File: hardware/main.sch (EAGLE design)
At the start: 69 parts, among them IC1 MPU-6050, IC2 TB6612FNG, Q1 TEFT4300, Q2 TEFT4300, Q3 TEFT4300, Q4 TEFT4300, Q5 TEFT4300, Q6 TEFT4300, Q8 8MHz

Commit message: schematic...
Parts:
- added C8_GRM1, C8_GRM2, C8_GRM3, C8_GRM31: 10u, rcl:C-EUC1206
- added C9_BYPASS, C9_BYPASS1: 100n, rcl:C-EUC0603
- added L1, L2: (no value), rcl:L-EUL5038P
- added Q7: IRLML2244, microbuilder:MOSFET-P
- added R22, R25: (no value), resistor:R-EU_R0805
- added R26, R27, R28, R29: (no value), rcl:R-EU_R0603
- added U$1: PRZELACZNIK_SUWAKOWY, micromouse:PRZELACZNIK_SUWAKOWY
- added U$2, U$3: PINHEAD-1X2, BaseApp:PINHEAD-1X2
- added U$4, U$5: ST1S40, micromouse:ST1S40
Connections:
- new net +7V: R22.2
- new net N$41: U$2.2, U$3.1
- new net N$43: U$1.2, U$1.5, U$3.2
- new net N$46: Q7.S, U$1.3, U$1.6
- new net N$47: L1.1, U$4.SW
- new net N$50: C8_GRM1.1, L1.2, R26.2
- new net N$52: R26.1, R27.2, U$4.FB
- new net N$53: R28.1, R29.2, U$5.FB
- new net N$54: C8_GRM3.1, L2.2, R28.2
- new net N$55: L2.1, U$5.SW
- new net VIN: C8_GRM2.1, C8_GRM31.1, C9_BYPASS.1, C9_BYPASS1.1, Q7.D, U$4.VINA, U$4.VINSW, U$5.VINA, U$5.VINSW
- net ADC_VBAT: now also R22.1, R25.2
- net GND: now also C8_GRM1.2, C8_GRM2.2, C8_GRM3.2, C8_GRM31.2, C9_BYPASS.2, C9_BYPASS1.2, Q7.G, R25.1, R27.1, R29.1, U$2.1, U$4.GND, U$5.GND
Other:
- moved on the sheet: C1, C12, C25, C3, C4, C5, C6, C7, C_VSSA, C_VSSA1, IC1, IC2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

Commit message: cleanup, 3d top mount
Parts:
- R10, R13, R15, R17, R21, R6, R8: value 1R -> 10k
- T1, T2, T3, T4, T5, T6, T8: value (none) -> IRLML0030
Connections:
- net LED5 renamed ENCL_A
- removed net N$1 (its old number): D7.A
- removed net N$11 (its old number): R8.1, T2.G
- removed net N$13 (its old number): D2.A
- removed net N$16: R10.1, T3.G
- removed net N$17: R13.1, T4.G
- removed net N$18: D4.A
- removed net N$21: R15.1, T5.G
- removed net N$22: D5.A
- removed net N$26: R17.1, T6.G
- removed net N$32: R21.1, T8.G
- removed net N$5 (its old number): D3.A
- removed net N$50: C8_GRM1.1, L1.2, R26.2
- removed net N$54: C8_GRM3.1, L2.2, R28.2
- removed net N$6 (its old number): R6.1, T1.G
- removed net N$8 (its old number): D1.A
- removed net VIN: C8_GRM2.1, C8_GRM31.1, C9_BYPASS.1, C9_BYPASS1.1, Q7.D, U$4.VINA, U$4.VINSW, U$5.VINA, U$5.VINSW
- new net ENCLB: U$6.PA1
- new net ENCR_A: U$6.PA15
- new net ENCR_B: U$6.PB3
- new net VCC: C8_GRM3.1, D1.A, D2.A, D3.A, D4.A, D5.A, D7.A, L2.2, R28.2
- net +3V3: now also C8_GRM1.1, L1.2, R26.2
- net +7V: now also C8_GRM2.1, C8_GRM31.1, C9_BYPASS.1, C9_BYPASS1.1, Q7.D, U$4.VINA, U$4.VINSW, U$5.VINA, U$5.VINSW
- net BOOT0: now also U$6.PB8; no longer U$6.PA15
- net BUZZER: now also R21.2, T8.G
- net D_L: now also T1.G; no longer U$6.PA1
- net D_LF: now also R15.2, T5.G; no longer R10.2
- net D_LS: now also R10.2, T3.G; no longer R15.2
- net D_R: now also T2.G
- net D_RF: now also R17.2, T6.G; no longer R13.2
- net D_RS: now also R13.2, T4.G; no longer R17.2, R21.2
- net GND: now also R10.1, R13.1, R15.1, R17.1, R21.1, R6.1, R8.1
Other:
- moved on the sheet: D2, D3, D4, D5, R10, R12, R13, R14, R15, R16, R17, R20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

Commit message: encoder brd
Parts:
- added U$10, U$9: ENCODER_MOUNT, micromouse:ENCODER_MOUNT
- added U$7, U$8: PINHEAD-1X2, BaseApp:PINHEAD-1X2
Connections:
- new net N$14: U$9.CLK
- new net N$15: U$9.MOSI
- new net N$16: U$9.MISO
- new net N$17: U$9.CS
- new net N$18: U$9.A
- new net N$19: U$9.B
- new net N$20: U$9.VCC
- new net N$22: U$10.A
- new net N$24: U$10.B
- new net N$25: U$10.VCC
- new net N$32: U$10.CS
- new net N$42: U$10.MISO
- new net N$44: U$10.MOSI
- new net N$45: U$10.CLK
- net GND: now also U$10.GND, U$9.GND
- net N$37: now also U$8.2
- net N$38: now also U$7.1
- net N$39: now also U$7.2
- net N$40: now also U$8.1
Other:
- moved on the sheet: C12, C5, C6, C7, IC2

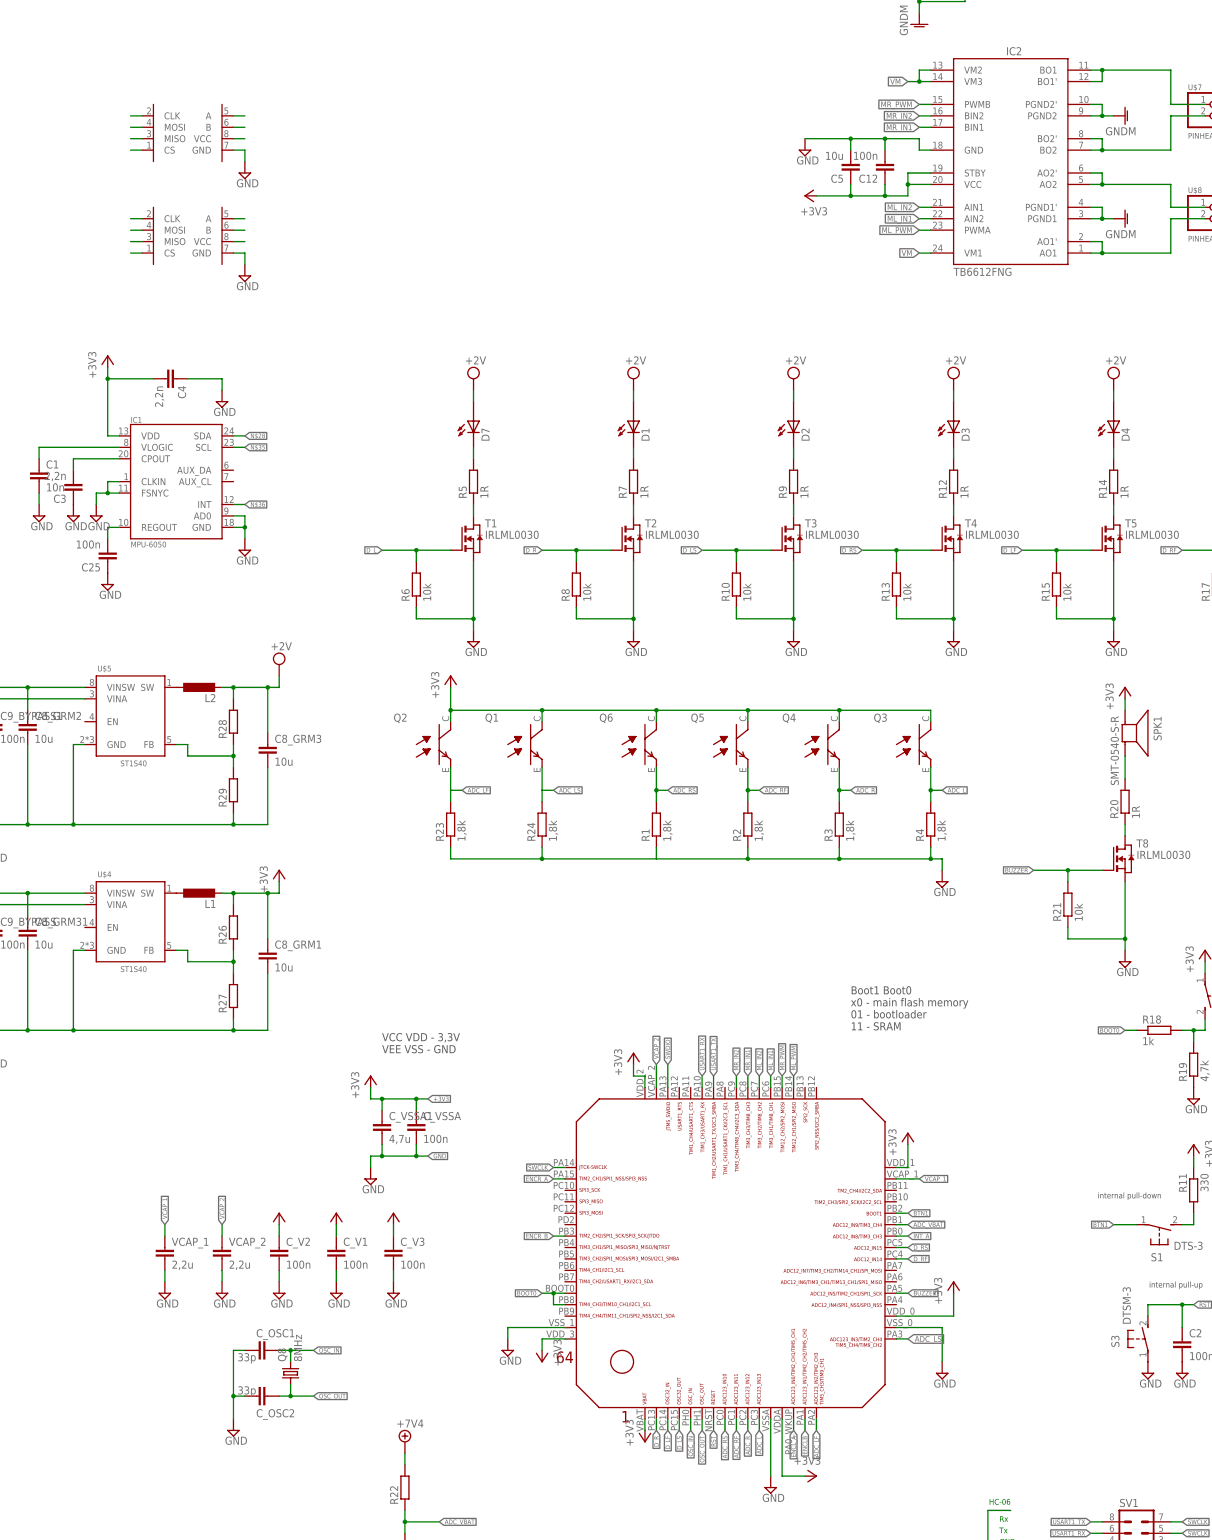
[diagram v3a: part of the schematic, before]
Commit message: fixed 3d model
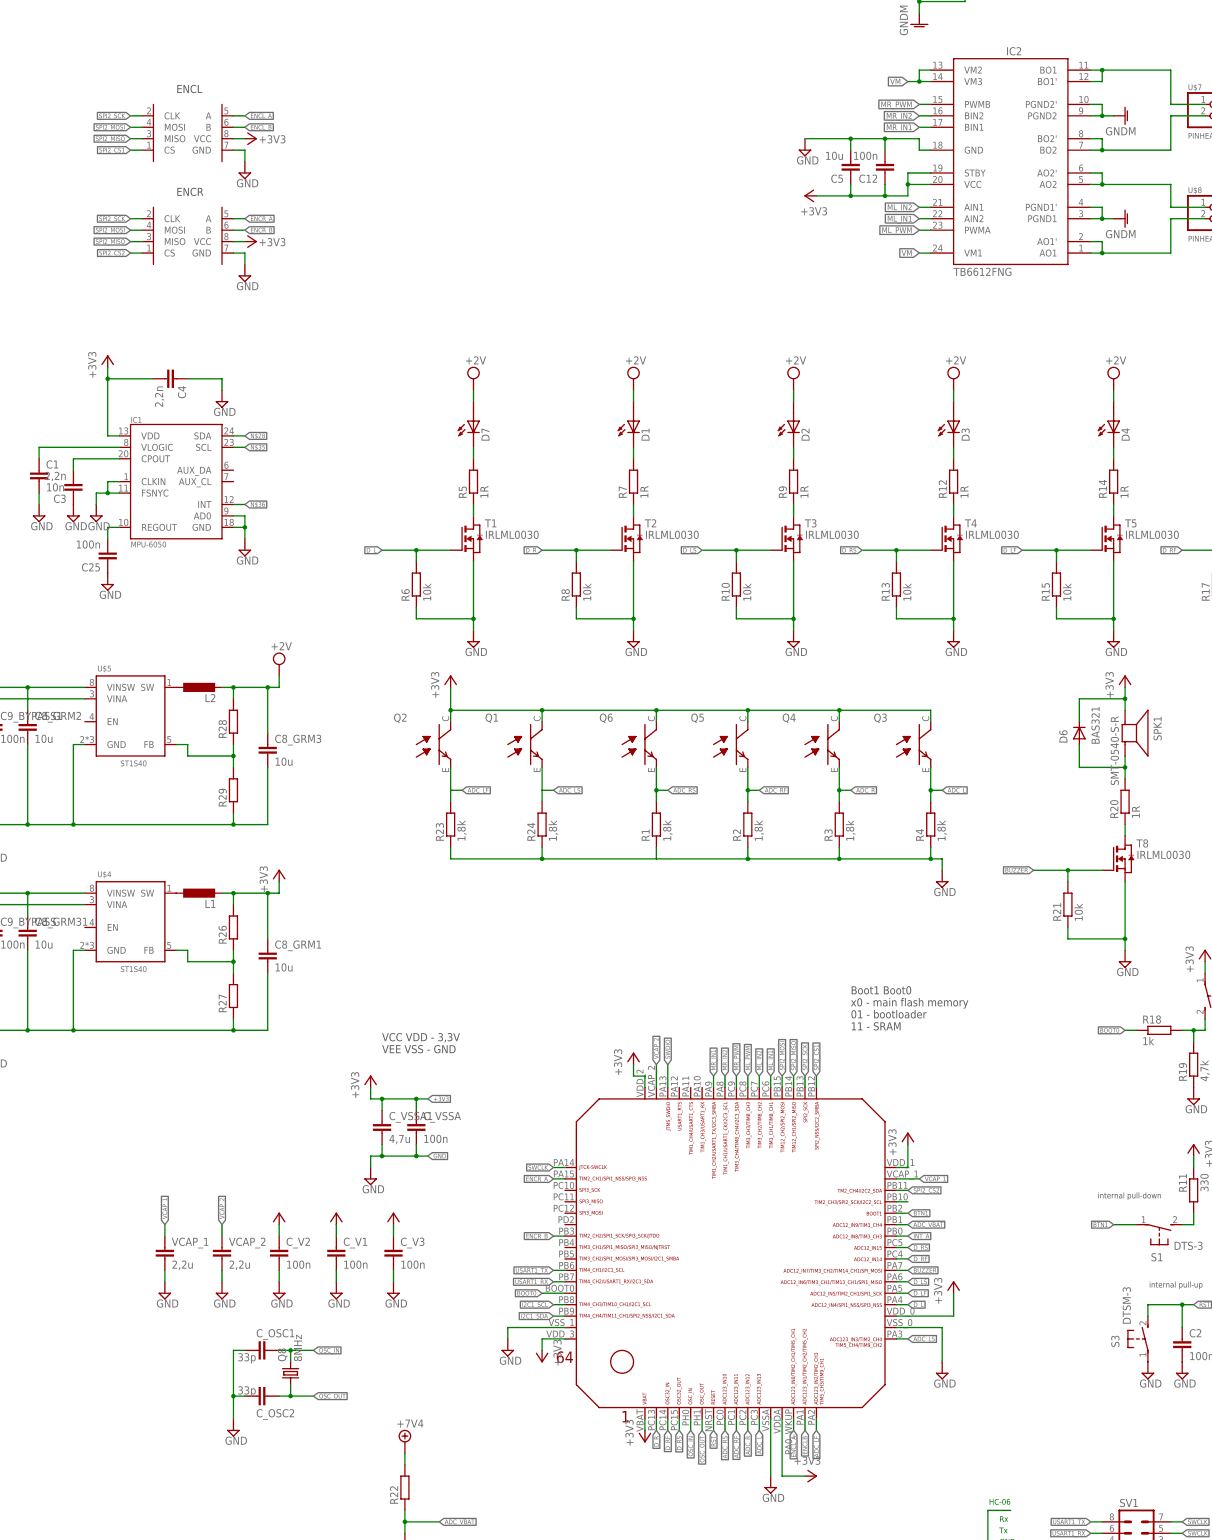
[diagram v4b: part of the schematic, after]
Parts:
- added D6: BAS321, nxp_60:BAS321
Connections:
- net N$19 renamed ENCL_B
- removed net N$14: U$9.CLK
- removed net N$15: U$9.MOSI
- removed net N$16: U$9.MISO
- removed net N$17: U$9.CS
- removed net N$18: U$9.A
- removed net N$20: U$9.VCC
- removed net N$22: U$10.A
- removed net N$24: U$10.B
- removed net N$25: U$10.VCC
- removed net N$32: U$10.CS
- removed net N$42: U$10.MISO
- removed net N$44: U$10.MOSI
- removed net N$45: U$10.CLK
- new net I2C1_SCL: U$6.PB8
- new net I2C1_SDA: U$6.PB9
- new net N$19: U$6.PB10
- new net SPI2_CS1: U$6.PB12, U$9.CS
- new net SPI2_CS2: U$10.CS, U$6.PB11
- new net SPI2_MISO: U$10.MISO, U$6.PB14, U$9.MISO
- new net SPI2_MOSI: U$10.MOSI, U$6.PB15, U$9.MOSI
- new net SPI2_SCK: U$10.CLK, U$6.PB13, U$9.CLK
- net +3V3: now also D6.K, U$10.VCC, U$9.VCC
- net BOOT0: no longer U$6.PB8
- net BUZZER: now also U$6.PA7; no longer U$6.PA5
- net D_L: now also U$6.PA4
- net D_LF: now also U$6.PA5; no longer U$6.PC14
- net D_LS: now also U$6.PA6; no longer U$6.PC15
- net D_RF: now also U$6.PC14
- net D_RS: now also U$6.PC15
- net ENCL_A: now also U$9.A
- net ENCR_A: now also U$10.A
- net ENCR_B: now also U$10.B
- net ML_PWM: now also U$6.PC8; no longer U$6.PB14
- net MR_IN1: now also U$6.PA9; no longer U$6.PC8
- net MR_IN2: now also U$6.PA8; no longer U$6.PC9
- net MR_PWM: now also U$6.PC9; no longer U$6.PB15
- net N$30: now also D6.A
- net USART1_RX: now also U$6.PB7; no longer U$6.PA10
- net USART1_TX: now also U$6.PB6; no longer U$6.PA9
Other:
- note added: "ENCL"
- note added: "ENCR"

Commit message: test
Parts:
- removed C8_GRM1, C8_GRM2, C8_GRM3, C8_GRM31: 10u, rcl:C-EUC1206
- removed C9_BYPASS, C9_BYPASS1: 100n, rcl:C-EUC0603
- removed C_OSC1, C_OSC2: 33p, rcl:C-EUC0603
- removed L1, L2: (no value), rcl:L-EUL5038P
- removed Q8: 8MHz, _microMouse:CRYSTAL_5X3.2MM
- removed R26, R27, R28, R29: (no value), rcl:R-EU_R0603
- removed S1, S2: DTS-3, switch-tact:DTS-3
- removed S3: DTSM-3, switch-tact:DTSM-3
- added C1_1, C1_2, C2_1, C2_2: 10u, rcl:C-EUC0805
- added C3_1, C3_2: 100n, rcl:C-EUC0603
- added L1_1: (no value), EAGLE-AECQ_PRODUCTS-rev17b:WE-MAIA_3015_78438335068
- added L1_2: (no value), EAGLE-AECQ_PRODUCTS-rev17b:WE-MAIA_3015_78438335033
- added Q9: IRLML2244, microbuilder:MOSFET-P
- added R1_1, R1_2, R2_1, R2_2: (no value), rcl:R-EU_R0603
- added R30, R31: 4k7, rcl:R-EU_R0603
- added R32: (no value), resistor:R-EU_R0805
- added R3_1, R3_2: 10k, rcl:R-EU_R0603
- added SW2, SW3, SW4: (no value), BaseApp:TACTILE-2PIN
- C_VSSA: value 100n -> 10n
- C_VSSA1: value 4,7u -> 1u
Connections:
- removed net N$19: U$6.PB10
- removed net N$28: IC1.SDA
- removed net N$35: IC1.SCL
- removed net N$47: L1.1, U$4.SW
- removed net N$55: L2.1, U$5.SW
- new net AGND: C_VSSA.2, C_VSSA1.2, R1.1, R2.1, R23.1, R24.1, R3.1, R4.1, U$6.VSSA
- new net DIV_EN: Q9.G, R32.1, U$6.PB10
- new net N$14: Q9.D, R22.2
- new net N$15: L1_1.1, U$5.SW
- new net N$16: L1_2.1, U$4.SW
- new net N$17: R3_1.1, U$5.EN
- new net N$18: R3_2.1, U$4.EN
- net +3V3: now also C2_2.1, L1_2.2, R1_2.2, R30.2, R31.2, SW3.1; no longer C8_GRM1.1, L1.2, R26.2, S2.1
- net +7V: now also C1_1.1, C1_2.1, C3_1.1, C3_2.1, Q9.S, R32.2, R3_1.2, R3_2.2; no longer C8_GRM2.1, C8_GRM31.1, C9_BYPASS.1, C9_BYPASS1.1, R22.2
- net BTN1: now also SW2.1; no longer S1.1
- net GND: now also C1_1.2, C1_2.2, C2_1.2, C2_2.2, C3_1.2, C3_2.2, R2_1.1, R2_2.1, SW4.1; no longer C8_GRM1.2, C8_GRM2.2, C8_GRM3.2, C8_GRM31.2, C9_BYPASS.2, C9_BYPASS1.2, C_OSC1.1, C_OSC2.1, C_VSSA.2, C_VSSA1.2, R1.1, R2.1, R23.1, R24.1, R27.1, R29.1, R3.1, R4.1, S3.1, U$6.VSSA
- net I2C1_SCL: now also IC1.SCL, R31.1
- net I2C1_SDA: now also IC1.SDA, R30.1
- net N$2: now also SW2.2; no longer S1.2
- net N$23: now also SW3.2; no longer S2.2
- net N$52: now also R1_2.1, R2_2.2; no longer R26.1, R27.2
- net N$53: now also R1_1.1, R2_1.2; no longer R28.1, R29.2
- net OSC_IN: no longer C_OSC1.2, Q8.2
- net OSC_OUT: no longer C_OSC2.2, Q8.1
- net RST: now also SW4.2; no longer S3.2
- net VCC: now also C2_1.1, L1_1.2, R1_1.2; no longer C8_GRM3.1, L2.2, R28.2
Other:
- note added: "CD00211314"
- moved on the sheet: R22, R25
